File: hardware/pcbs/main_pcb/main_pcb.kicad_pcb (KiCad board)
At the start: 2 copper layers, 130 x 100 mm, 57 parts, among them J2 Conn_01x07, J3 Conn_01x07, J4 Conn_01x13, J5 Conn_01x06, J6 Conn_01x02, J7 USB_C_Receptacle_USB2.0_14P, SW1 SW_Push, U1 TXB0104D, U2 TXB0104D, U3 TXB0104D, U4 AMS1117-3.3, U5 ATmega2560-16A, U6 CH340C, Y1 Crystal_GND24

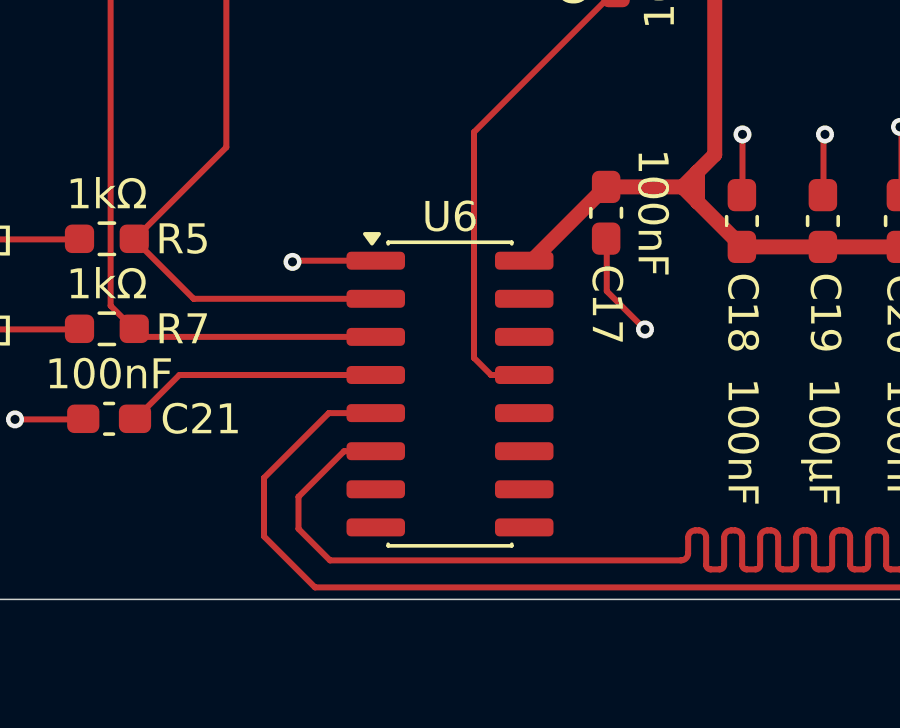
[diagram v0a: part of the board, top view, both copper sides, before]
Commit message: fix: swaps CH340C because KiCad keeps swapping it for the default one (#127)
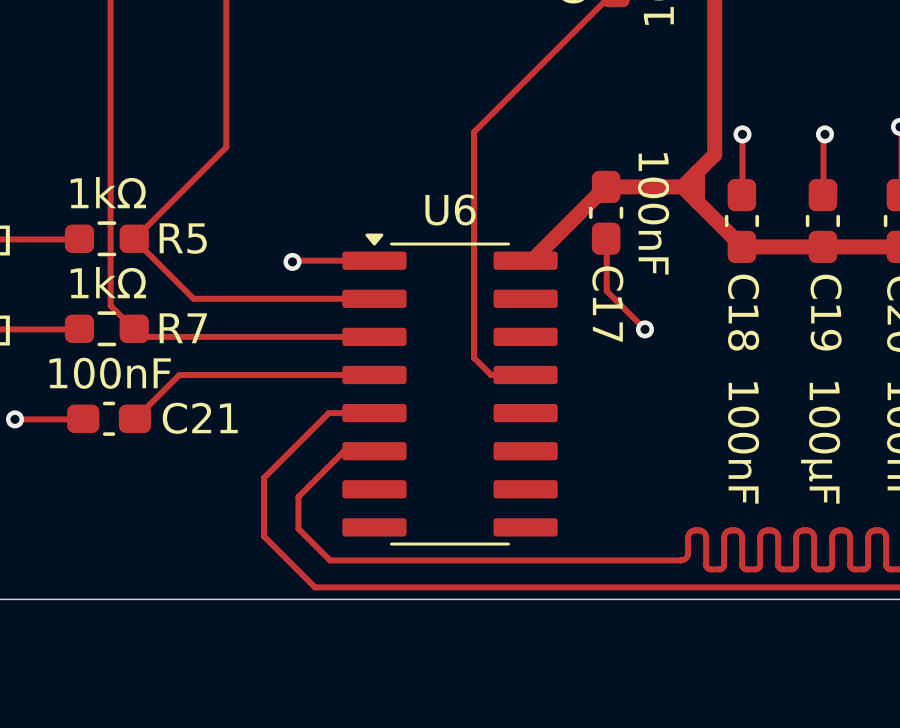
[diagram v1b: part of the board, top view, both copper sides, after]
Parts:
- U6: footprint Package_SO:SOIC-16_3.9x9.9mm_P1.27mm -> Lilibrary:SOP-16_CH340C
